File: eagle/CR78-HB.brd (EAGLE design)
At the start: 100.6 x 80.6 mm, 34 parts, among them Q1 2N3904, Q2 2N3904, Q3 2N3904, X1 22-23-2021

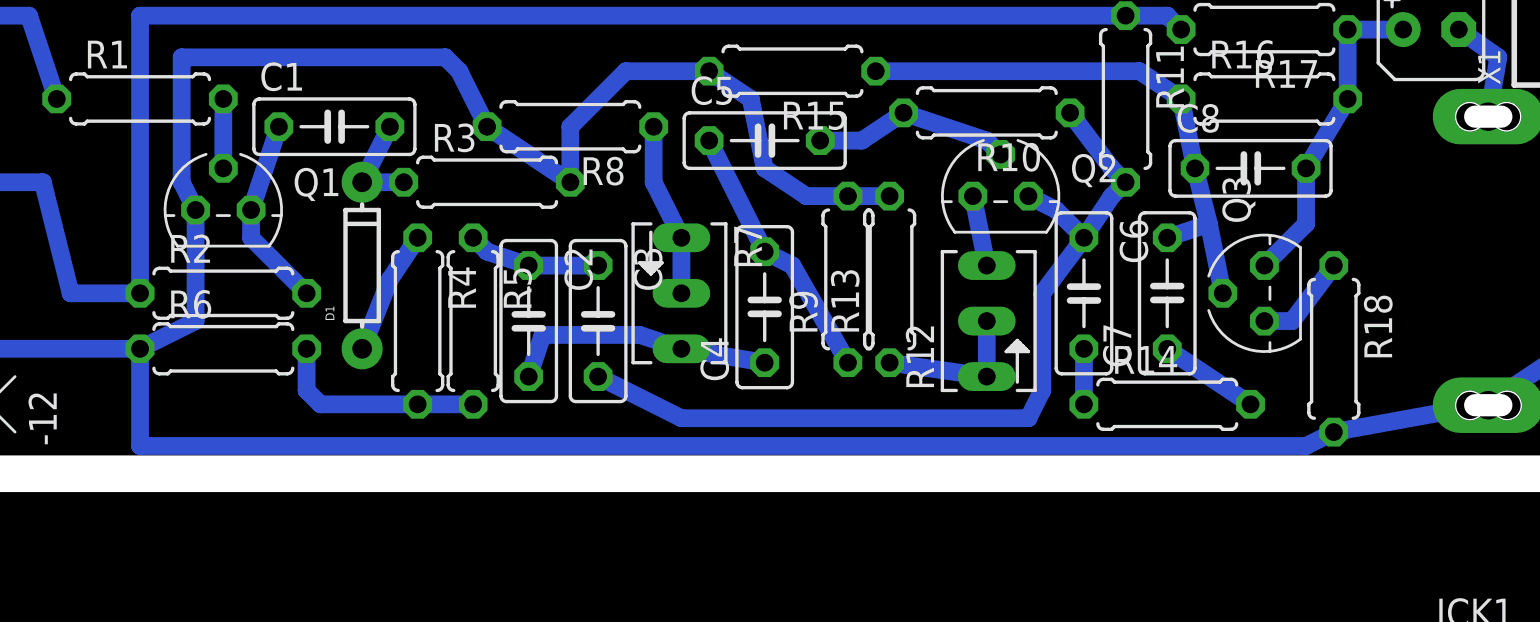
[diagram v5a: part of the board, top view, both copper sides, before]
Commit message: added output pulldown 10k for bd
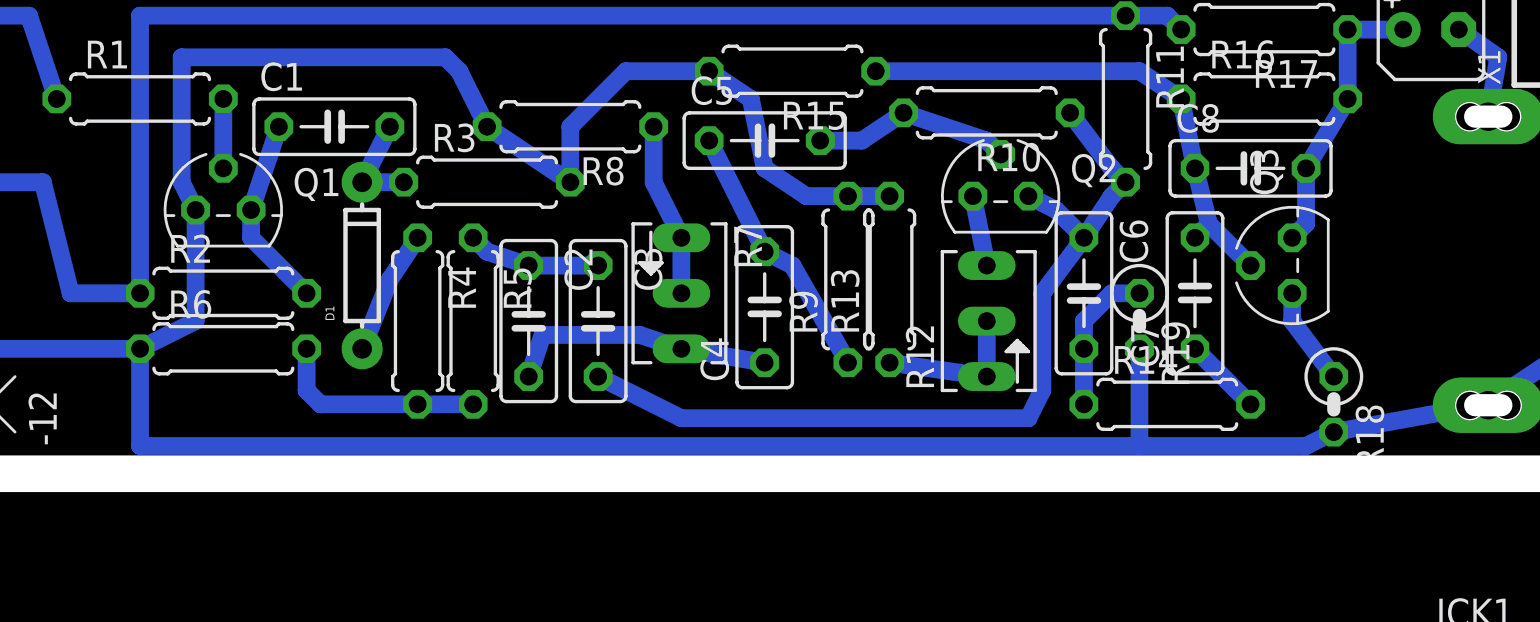
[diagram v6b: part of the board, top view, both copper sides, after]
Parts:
- added R19: 10k, rcl:0207/2V
- C2: value 22n -> 82n
- C3: value 27n -> 82n
- C4, C5: value 22n -> 68n
- C6: value 10n -> 27n
- R14: value 560k -> 18k
- R18: device rcl:0207/7 -> rcl:0207/2V
- R4: value 390k -> 150k
- moved R18 2.54 mm to (67.3, 2.54)
- moved Q3 1.80 mm to (65.4, 8.89)
- moved C7 1.27 mm to (61.0, 7.62)
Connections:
- net GND: now also R19.2
- net N$14: now also R19.1
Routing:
- net GND: track 168.9 -> 173.4 mm
- net N$14: track 2.54 -> 6.88 mm
- net N$16: track 14.7 -> 12.9 mm
- net N$18: track 25.5 -> 23.8 mm
- net N$17: track 4.58 -> 3.59 mm
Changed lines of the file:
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@@
 <elements>
 <element name="C1" library="rcl" package="C050-025X075" value="27n" x="21.59" y="15.24"/>
-<element name="C2" library="rcl" package="C050-025X075" value="22n" x="30.48" y="6.35" rot="R270"/>
-<element name="C3" library="rcl" package="C050-025X075" value="27n" x="33.655" y="6.35" rot="R270"/>
-<element name="C4" library="rcl" package="C050-025X075" value="22n" x="41.275" y="6.985" rot="R90"/>
-<element name="C5" library="rcl" package="C050-025X075" value="22n" x="41.275" y="14.605"/>
-<element name="C6" library="rcl" package="C050-025X075" value="10n" x="55.88" y="7.62" rot="R270"/>
-<element name="C7" library="rcl" package="C050-025X075" value="473" x="59.69" y="7.62" rot="R90"/>
+<element name="C2" library="rcl" package="C050-025X075" value="82n" x="30.48" y="6.35" rot="R270"/>
+<element name="C3" library="rcl" package="C050-025X075" value="82n" x="33.655" y="6.35" rot="R270"/>
+<element name="C4" library="rcl" package="C050-025X075" value="68n" x="41.275" y="6.985" rot="R90"/>
+<element name="C5" library="rcl" package="C050-025X075" value="68n" x="41.275" y="14.605"/>
+<element name="C6" library="rcl" package="C050-025X075" value="27n" x="55.88" y="7.62" rot="R270"/>
+<element name="C7" library="rcl" package="C050-025X075" value="473" x="60.96" y="7.62" rot="R90"/>
 <element name="C8" library="rcl" package="C050-025X075" value="47p" x="63.5" y="13.335"/>
 <element name="C9" library="rcl" package="B45181A" value="1uF" x="71.755" y="19.685"/>
@@
 <element name="Q2" library="808_lt" package="TO92" value="2N3904" x="52.07" y="12.065"/>
 <element name="Q1" library="808_lt" package="TO92" value="2N3904" x="16.51" y="11.43"/>
-<element name="Q3" library="808_lt" package="TO92" value="2N3904" x="64.135" y="7.62" rot="R90"/>
+<element name="Q3" library="808_lt" package="TO92" value="2N3904" x="65.405" y="8.89" rot="R90"/>
 <element name="R3" library="rcl" package="0207/7" value="270k" x="28.575" y="12.7"/>
-<element name="R14" library="rcl" package="0207/7" value="560k" x="59.69" y="2.54"/>
+<element name="R14" library="rcl" package="0207/7" value="18k" x="59.69" y="2.54"/>
 <element name="R16" library="rcl" package="0207/7" value="470k" x="64.135" y="16.51"/>
 <element name="R17" library="rcl" package="0207/7" value="47k" x="64.135" y="19.685" rot="R180"/>
-<element name="R18" library="rcl" package="0207/7" value="220R" x="67.31" y="5.08" rot="R270"/>
+<element name="R18" library="rcl" package="0207/2V" value="220R" x="67.31" y="2.54" rot="R270"/>
 <element name="R15" library="rcl" package="0207/7" value="100k" x="42.545" y="17.78" rot="R180"/>
-<element name="R4" library="rcl" package="0207/7" value="390k" x="25.4" y="6.35" rot="R270"/>
+<element name="R4" library="rcl" package="0207/7" value="150k" x="25.4" y="6.35" rot="R270"/>
 <element name="R6" library="rcl" package="0207/7" value="56k" x="16.51" y="5.08"/>
 <element name="R2" library="rcl" package="0207/7" value="10k" x="16.51" y="7.62"/>
@@
 <element name="R12" library="TR808clone" package="B64Y" value="500R" x="51.435" y="6.35" rot="R90"/>
 <element name="R7" library="TR808clone" package="B64Y" value="10KB" x="37.465" y="7.62" rot="R270"/>
+<element name="R19" library="rcl" package="0207/2V" value="10k" x="58.42" y="6.35" rot="R270"/>
 </elements>
 <signals>
@@
 <wire x1="26.67" y1="18.415" x2="14.605" y2="18.415" width="0.8128" layer="16"/>
 <wire x1="66.04" y1="0.635" x2="67.31" y2="1.27" width="0.8128" layer="16"/>
-<wire x1="12.7" y1="0.635" x2="66.04" y2="0.635" width="0.8128" layer="16"/>
+<wire x1="12.7" y1="0.635" x2="58.42" y2="0.635" width="0.8128" layer="16"/>
+<wire x1="58.42" y1="0.635" x2="66.04" y2="0.635" width="0.8128" layer="16"/>
 <wire x1="12.7" y1="5.08" x2="12.7" y2="0.635" width="0.8128" layer="16"/>
 <wire x1="41.275" y1="13.335" x2="43.18" y2="12.065" width="0.8128" layer="16"/>
@@
 <wire x1="41.275" y1="13.335" x2="40.64" y2="16.51" width="0.8128" layer="16"/>
 <wire x1="40.64" y1="16.51" x2="38.735" y2="17.78" width="0.8128" layer="16"/>
+<contactref element="R19" pad="2"/>
+<wire x1="58.42" y1="5.08" x2="58.42" y2="0.635" width="0.8128" layer="16"/>
 <wire x1="74.295" y1="2.54" x2="74.375" y2="2.5" width="0" layer="19" extent="16-16"/>
 </signal>
@@
 <contactref element="C6" pad="2"/>
 <wire x1="55.88" y1="2.54" x2="55.88" y2="5.08" width="0.8128" layer="16"/>
+<contactref element="R19" pad="1"/>
+<wire x1="55.88" y1="5.08" x2="55.88" y2="6.35" width="0.8128" layer="16"/>
+<wire x1="55.88" y1="6.35" x2="57.15" y2="7.62" width="0.8128" layer="16"/>
+<wire x1="57.15" y1="7.62" x2="58.42" y2="7.62" width="0.8128" layer="16"/>
 </signal>
 <signal name="N$15">
 <contactref element="Q3" pad="3"/>
 <contactref element="R18" pad="1"/>
-<wire x1="65.405" y1="6.35" x2="64.135" y2="6.35" width="0.8128" layer="16"/>
-<wire x1="67.31" y1="8.89" x2="65.405" y2="6.35" width="0.8128" layer="16"/>
+<wire x1="65.405" y1="6.35" x2="65.405" y2="7.62" width="0.8128" layer="16"/>
+<wire x1="67.31" y1="3.81" x2="65.405" y2="6.35" width="0.8128" layer="16"/>
 </signal>
 <signal name="N$12">
@@
 <contactref element="C9" pad="+"/>
 <wire x1="66.04" y1="13.335" x2="66.04" y2="10.795" width="0.8128" layer="16"/>
-<wire x1="66.04" y1="10.795" x2="64.135" y2="8.89" width="0.8128" layer="16"/>
+<wire x1="66.04" y1="10.795" x2="65.405" y2="10.16" width="0.8128" layer="16"/>
 <wire x1="67.945" y1="19.685" x2="67.945" y2="16.51" width="0.8128" layer="16"/>
 <wire x1="67.945" y1="19.685" x2="70.485" y2="19.685" width="0.8128" layer="16"/>
@@
 <contactref element="R14" pad="2"/>
 <contactref element="C7" pad="1"/>
-<wire x1="63.5" y1="2.54" x2="59.69" y2="5.08" width="0.8128" layer="16"/>
+<wire x1="63.5" y1="2.54" x2="60.96" y2="5.08" width="0.8128" layer="16"/>
 </signal>
 <signal name="N$18">
@@
 <contactref element="Q3" pad="2"/>
 <contactref element="R15" pad="1"/>
-<wire x1="62.23" y1="7.62" x2="61.595" y2="10.795" width="0.8128" layer="16"/>
+<wire x1="63.5" y1="8.89" x2="61.595" y2="10.795" width="0.8128" layer="16"/>
 <wire x1="61.595" y1="10.795" x2="60.96" y2="13.335" width="0.8128" layer="16"/>
 <wire x1="58.42" y1="17.78" x2="46.355" y2="17.78" width="0.8128" layer="16"/>
 <wire x1="60.325" y1="16.51" x2="58.42" y2="17.78" width="0.8128" layer="16"/>
 <wire x1="60.325" y1="16.51" x2="60.96" y2="13.335" width="0.8128" layer="16"/>
-<wire x1="59.69" y1="10.16" x2="61.595" y2="10.795" width="0.8128" layer="16"/>
+<wire x1="60.96" y1="10.16" x2="61.595" y2="10.795" width="0.8128" layer="16"/>
 </signal>
 <signal name="N$19">

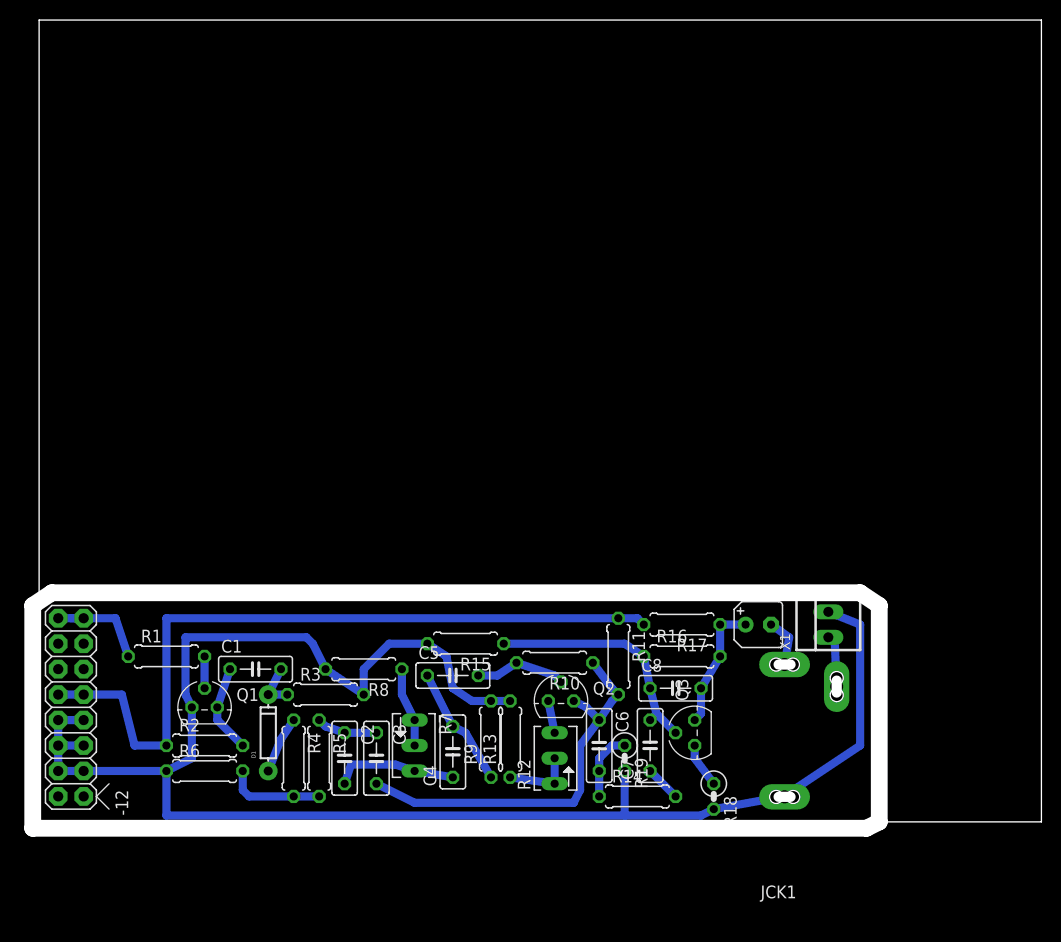
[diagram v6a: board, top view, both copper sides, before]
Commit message: routed with panel pots
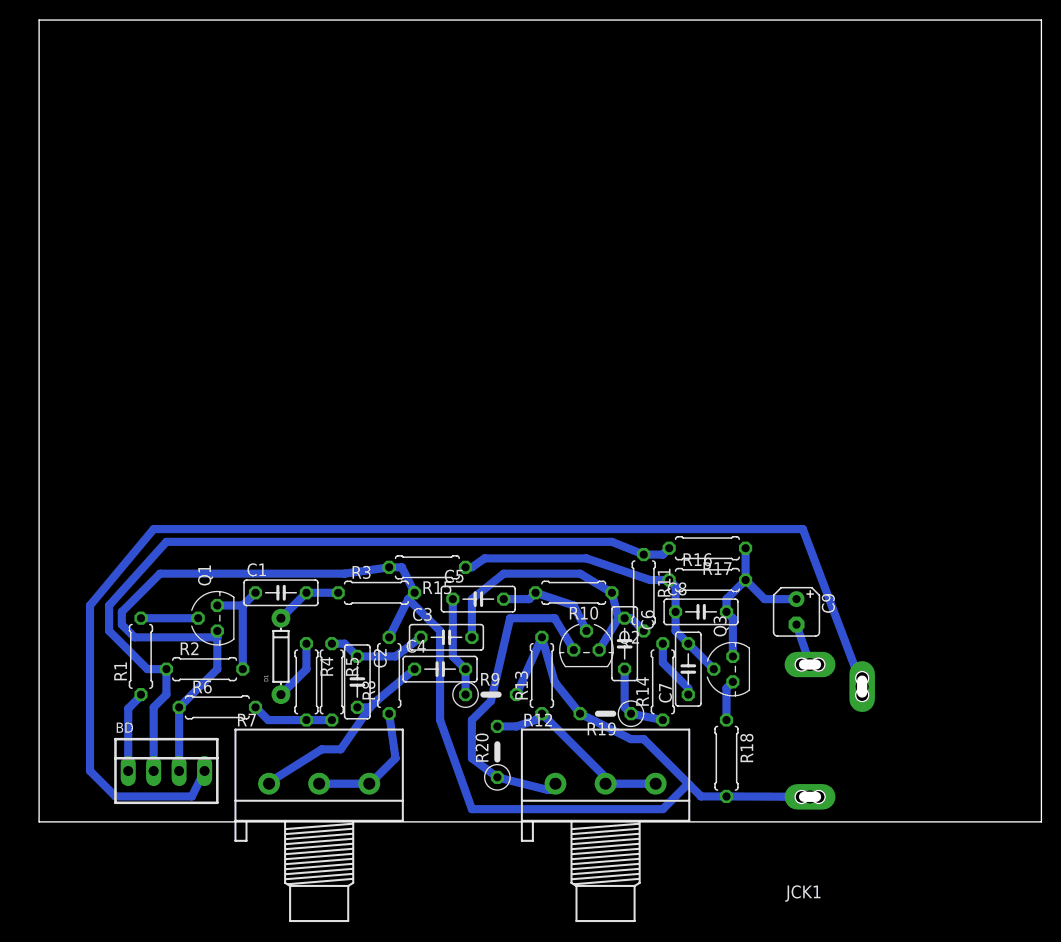
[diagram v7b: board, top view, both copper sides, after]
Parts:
- removed PWR1: POWER, eurorack:POWER_16
- removed X1: 22-23-2021, con-molex:22-23-2021
- added BD: 22-23-2041, con-molex:22-23-2041
- added R20: 15k, rcl:0207/5V
- R12, R7: device TR808clone:B64Y -> pot:3RP/1610N
- R18: device rcl:0207/2V -> rcl:0207/7
- R19: device rcl:0207/2V -> rcl:0207/5V
- R9: device rcl:0207/7 -> rcl:0207/5V
- moved C3 13.9 mm to (40.6, 18.4), turned to 0 degrees
- moved R14 11.7 mm to (62.2, 14.0), turned to 90 degrees
- moved R3 11.4 mm to (33.7, 22.9)
- moved C6 10.5 mm to (58.4, 17.8)
- moved R7 10.3 mm to (27.9, 3.81), turned to 0 degrees
- moved Q1 8.98 mm to (17.8, 20.3), turned to 90 degrees
- moved R15 8.52 mm to (38.7, 25.4)
- moved C7 8.52 mm to (64.8, 15.2)
- moved C4 8.35 mm to (40.0, 15.2), turned to 0 degrees
- moved C1 8.03 mm to (24.1, 22.9)
- moved C5 8.03 mm to (43.8, 22.2)
- moved C8 8.03 mm to (66.0, 21.0)
- moved R17 8.03 mm to (66.7, 27.3)
- moved R16 8.03 mm to (66.7, 24.1)
- moved R4 7.73 mm to (26.7, 14.0)
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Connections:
- net +12V: now also BD.2; no longer PWR1.10, PWR1.9
- net GND: now also BD.3; no longer PWR1.3, PWR1.4, PWR1.5, PWR1.6, PWR1.7, PWR1.8, X1.2
- net N$11: now also BD.1; no longer PWR1.15, PWR1.16
- net N$12: now also BD.4; no longer X1.1
- net N$13: now also R12.1, R20.1; no longer R12.A
- net N$5: now also R7.2, R7.3; no longer R7.E, R7.S
- net N$6: now also R7.1; no longer R7.A
- net N$8: now also R12.2, R12.3, R20.2; no longer R12.E, R12.S
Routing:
- net N$12: track 5.34 -> 122.0 mm
- net N$13: track 3.24 -> 32.5 mm
- net GND: track 173.4 -> 150.7 mm
- net N$8: track 7.03 -> 19.7 mm
- net N$9: track 39.7 -> 28.6 mm
- net N$6: track 12.3 -> 20.8 mm
- net N$18: track 23.8 -> 31.7 mm
- net N$5: track 7.92 -> 13.2 mm
- net N$16: track 12.9 -> 17.7 mm
- net +12V: track 75.3 -> 79.7 mm
- net N$4: track 6.08 -> 10.1 mm
- net N$11: track 11.0 -> 8.15 mm
- net N$17: track 3.59 -> 6.13 mm
- net N$47: track 3.18 -> 5.71 mm
- net N$10: track 12.2 -> 10.1 mm
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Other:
- board size 100.6 x 80.6 mm -> 100 x 80 mm

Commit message: tweaks
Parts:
- moved C9 1.93 mm to (73.8, 20.2)
- moved R6 1.63 mm to (19.1, 10.4)
- moved R2 1.27 mm to (17.8, 15.2)
- moved R1 1.02 mm to (11.2, 16.5)
- moved R11 0.92 mm to (60.8, 23.6)
- moved C4 0.51 mm to (40.5, 15.2)
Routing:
- net N$12: track 122.0 -> 118.4 mm
- net N$13: track 32.5 -> 30.9 mm
- net N$16: track 17.7 -> 16.1 mm
- net N$3: track 8.15 -> 6.60 mm
- net GND: track 150.7 -> 149.6 mm
- net N$47: track 5.71 -> 4.70 mm
- net N$5: track 13.2 -> 12.3 mm
- net +12V: track 79.7 -> 80.5 mm
- net N$6: track 20.8 -> 20.2 mm
